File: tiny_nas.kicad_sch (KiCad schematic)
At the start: 110 parts, among them J1 Conn_02x07_Odd_Even, J2 DM3AT-SF-PEJM5, J3 USB_B_Micro, J4 Conn_01x02_Male, J5 HR911105A, J6 USB_B_Micro, J7 USB_B_Micro, J8 Conn_01x02_Male, J9 Conn_01x02_Male, SW1 SW_SPDT, U1 AMS1117-3.3, U2 LAN8720A, U3 STM32F407ZGTx, U4 USBLC6-4SC6, U5 USB3300-EZK, U6 MAX1823BEUB, U7 CH340E, Y1 16MHz, Y2 25MHz, Y3 24MHz

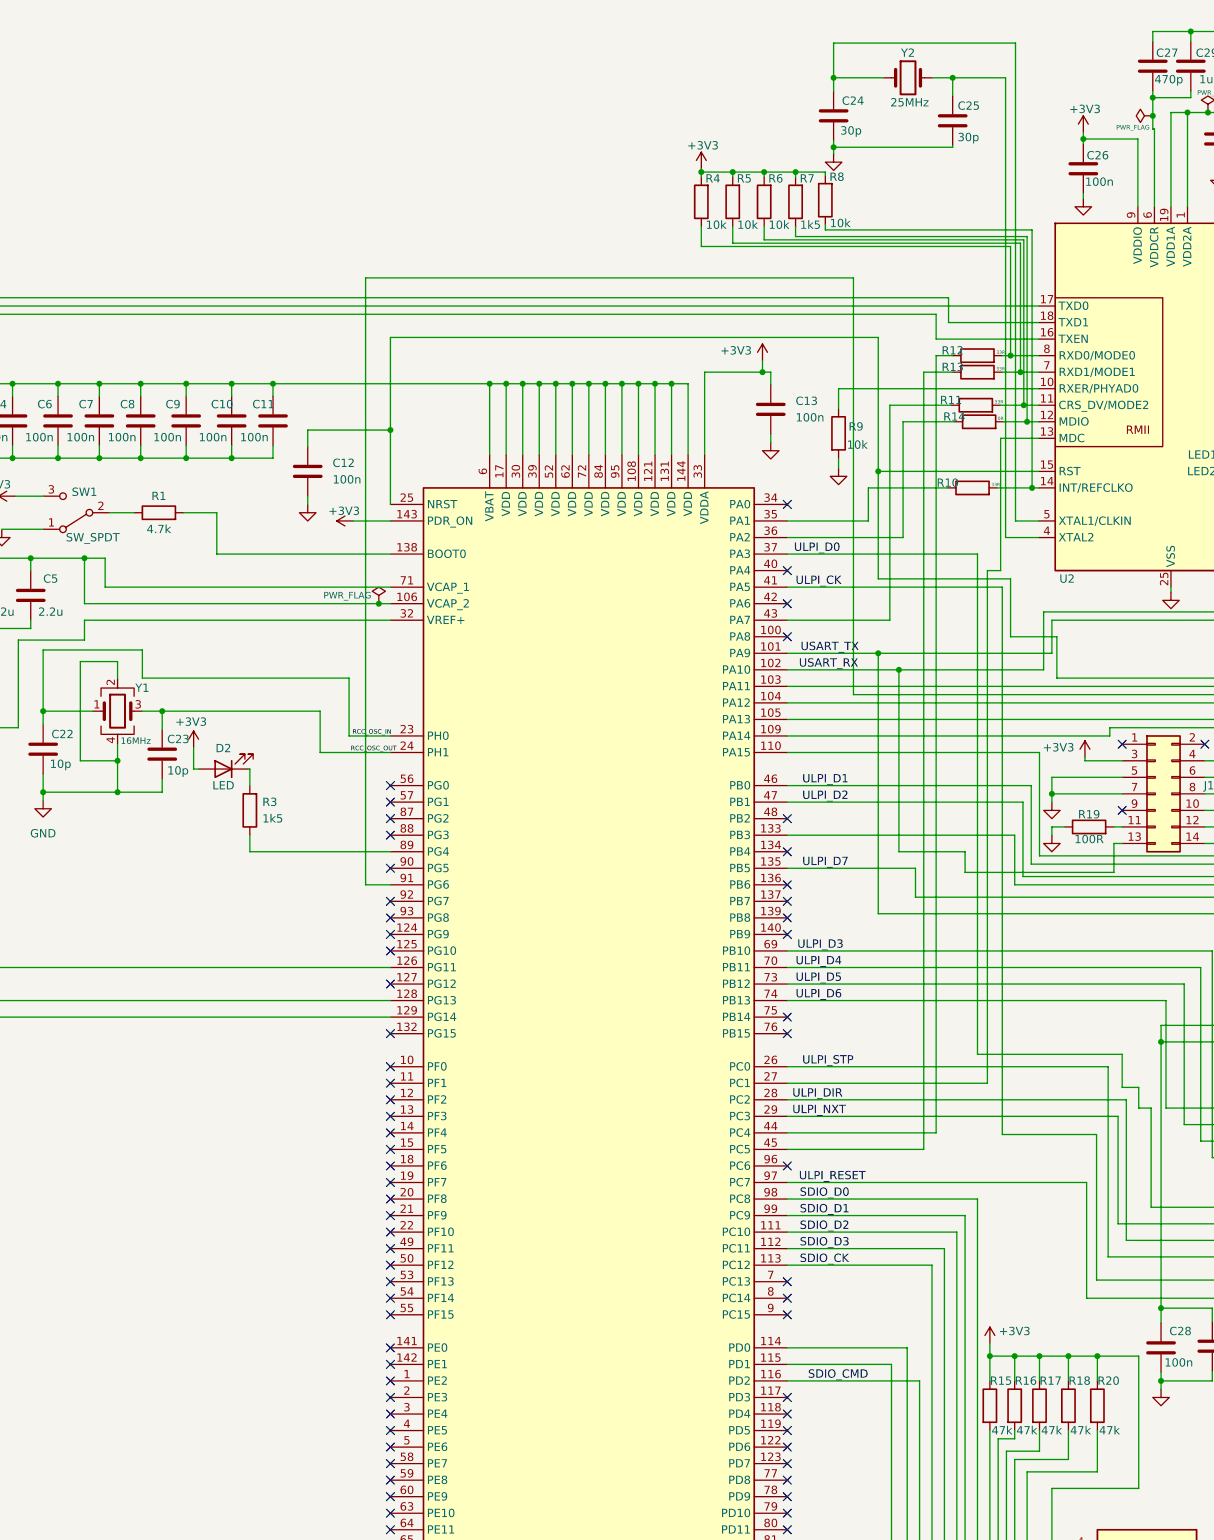
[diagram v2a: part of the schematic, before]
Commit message: Added Ethernet PHY reset GPIO and pin header to choose input clock from MCO or crystal
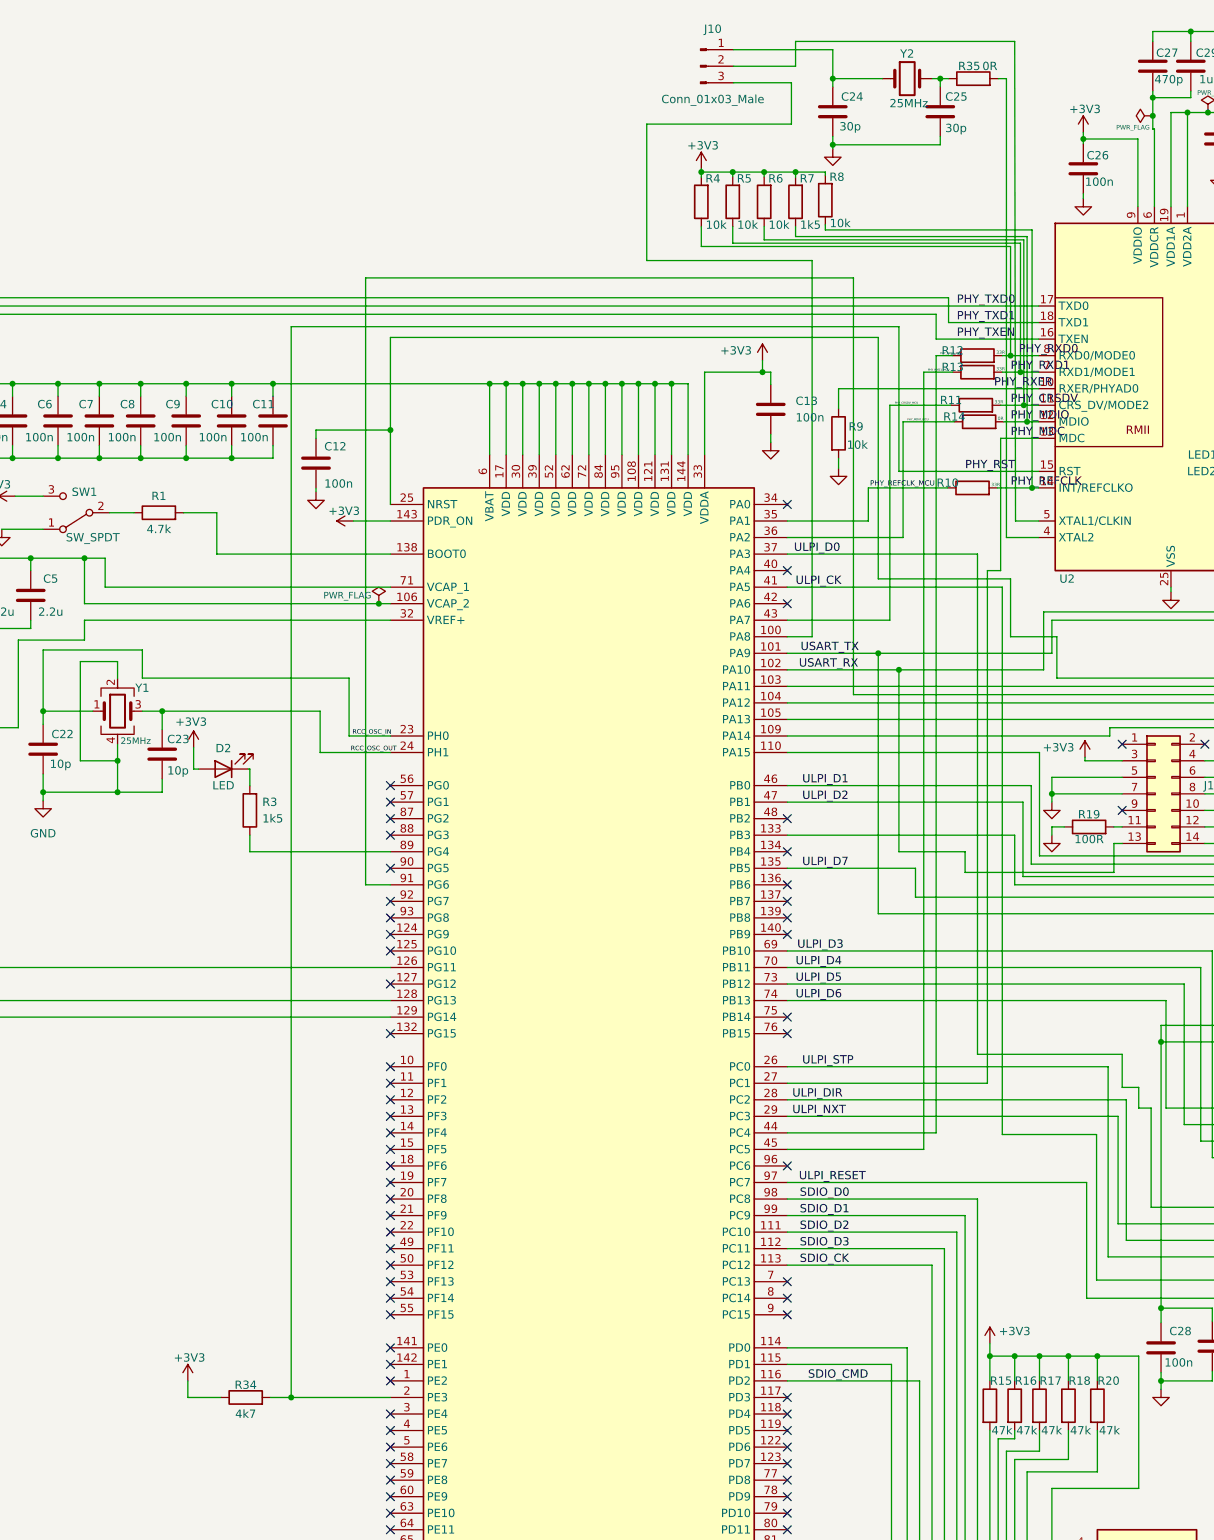
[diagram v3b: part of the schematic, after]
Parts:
- added J10: Conn_01x03_Male, Connector_PinHeader_2.54mm:PinHeader_1x03_P2.54mm_Vertical, symbol Connector:Conn_01x03_Male
- added R34: 4k7, Resistor_SMD:R_0402_1005Metric, symbol Device:R
- added R35: 0R, Resistor_SMD:R_0402_1005Metric, symbol Device:R
- Y1: value 16MHz -> 25MHz
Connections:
- net +3V3: now also R34.1
- net PHY_CRSDV_MCU: now reaches R11.1, U3.43 (PA7)
- net PHY_CRSDV: now reaches R11.2, R6.1, U2.11 (CRS_DV/MODE2)
- net PHY_RXD0_MCU: now reaches R12.1, U3.44 (PC4)
- net PHY_RXD0: now reaches R12.2, R4.1, U2.8 (RXD0/MODE0)
- net PHY_REFCLK_MCU: now reaches R10.1, U3.35 (PA1)
- net PHY_REFCLK: now reaches R10.2, R8.1, U2.14 (INT/REFCLKO)
- net at C12.2, J1.12 (Pin_12), U3.25 (NRST): no longer U2.15 (RST)
- net at C25.1, Y2.2: now also R35.1; no longer U2.4 (XTAL2)
- net PHY_RXER: now reaches R9.1, U2.10 (RXER/PHYAD0)
- net PHY_MDIO: now reaches R14.2, R7.1, U2.12 (MDIO)
- net PHY_MDC: now reaches U2.13 (MDC), U3.27 (PC1)
- net PHY_TXEN: now reaches U2.16 (TXEN), U3.126 (PG11)
- net PHY_TXD0: now reaches U2.17 (TXD0), U3.128 (PG13)
- net PHY_TXD1: now reaches U2.18 (TXD1), U3.129 (PG14)
- net at C24.1, Y2.1: now also J10.1 (Pin_1); no longer U2.5 (XTAL1/CLKIN)
- net PHY_RXD1: now reaches R13.2, R5.1, U2.7 (RXD1/MODE1)
- net PHY_MDIO_MCU: now reaches R14.1, U3.36 (PA2)
- net at U3.100 (PA8): now also J10.3 (Pin_3)
- net PHY_RST: now reaches U3.2 (PE3)
- net PHY_RST: now also U2.15 (RST), R34.2
- net PHY_RXD1_MCU: now reaches R13.1, U3.45 (PC5)
- new net: R35.2, U2.4 (XTAL2)
- new net: J10.2 (Pin_2), U2.5 (XTAL1/CLKIN)
- no-connect marks 84 -> 82
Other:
- moved on the sheet: C12, C24, C25

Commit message: change resistors footprint, add manufacturing files
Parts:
- R14, R26, R27, R30, R33, R35: footprint Resistor_SMD:R_0402_1005Metric -> Resistor_SMD:R_0603_1608Metric
- R22, R24, R25, R28: value 50R -> 49.9R; footprint Resistor_SMD:R_0402_1005Metric -> Resistor_SMD:R_0805_2012Metric
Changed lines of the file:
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@@
     (property "Reference" "R26" (id 0) (at 312.674 89.408 90))
     (property "Value" "270R" (id 1) (at 312.674 93.472 90))
-    (property "Footprint" "Resistor_SMD:R_0402_1005Metric" (id 2) (at 312.674 93.218 90)
+    (property "Footprint" "Resistor_SMD:R_0603_1608Metric" (id 2) (at 312.674 93.218 90)
       (effects (font (size 1.27 1.27)) hide)
     )
@@
       (effects (font (size 1.27 1.27)) (justify left))
     )
-    (property "Value" "50R" (id 1) (at 286.512 24.384 0)
-      (effects (font (size 1.27 1.27)) (justify left))
+    (property "Value" "49.9R" (id 1) (at 286.512 24.384 0)
+      (effects (font (size 1 1)) (justify left))
     )
-    (property "Footprint" "Resistor_SMD:R_0402_1005Metric" (id 2) (at 284.226 20.32 90)
+    (property "Footprint" "Resistor_SMD:R_0805_2012Metric" (id 2) (at 284.226 20.32 90)
       (effects (font (size 1.27 1.27)) hide)
     )
@@
       (effects (font (size 1.27 1.27)) (justify left))
     )
-    (property "Value" "50R" (id 1) (at 301.244 24.892 0)
-      (effects (font (size 1.27 1.27)) (justify left))
+    (property "Value" "49.9R" (id 1) (at 300.99 24.384 0)
+      (effects (font (size 0.8 0.8)) (justify left))
     )
-    (property "Footprint" "Resistor_SMD:R_0402_1005Metric" (id 2) (at 298.958 20.828 90)
+    (property "Footprint" "Resistor_SMD:R_0805_2012Metric" (id 2) (at 298.958 20.828 90)
       (effects (font (size 1.27 1.27)) hide)
     )
@@
     (property "Reference" "R33" (id 0) (at 327.406 198.628 90))
     (property "Value" "0R" (id 1) (at 327.406 202.692 90))
-    (property "Footprint" "Resistor_SMD:R_0402_1005Metric" (id 2) (at 327.406 202.438 90)
+    (property "Footprint" "Resistor_SMD:R_0603_1608Metric" (id 2) (at 327.406 202.438 90)
       (effects (font (size 1.27 1.27)) hide)
     )
@@
     (property "Reference" "R27" (id 0) (at 313.182 76.962 90))
     (property "Value" "270R" (id 1) (at 313.182 81.28 90))
-    (property "Footprint" "Resistor_SMD:R_0402_1005Metric" (id 2) (at 313.436 80.772 90)
+    (property "Footprint" "Resistor_SMD:R_0603_1608Metric" (id 2) (at 313.436 80.772 90)
       (effects (font (size 1.27 1.27)) hide)
     )
@@
       (effects (font (size 1.27 1.27)) (justify left))
     )
-    (property "Value" "50R" (id 1) (at 291.846 24.384 0)
-      (effects (font (size 1.27 1.27)) (justify left))
+    (property "Value" "49.9R" (id 1) (at 291.846 24.384 0)
+      (effects (font (size 1 1)) (justify left))
     )
-    (property "Footprint" "Resistor_SMD:R_0402_1005Metric" (id 2) (at 289.56 20.32 90)
+    (property "Footprint" "Resistor_SMD:R_0805_2012Metric" (id 2) (at 289.56 20.32 90)
       (effects (font (size 1.27 1.27)) hide)
     )
@@
       (effects (font (size 1.27 1.27)) (justify left))
     )
-    (property "Value" "50R" (id 1) (at 297.18 24.638 0)
-      (effects (font (size 1.27 1.27)) (justify left))
+    (property "Value" "49.9R" (id 1) (at 296.672 24.384 0)
+      (effects (font (size 0.8 0.8)) (justify left))
     )
-    (property "Footprint" "Resistor_SMD:R_0402_1005Metric" (id 2) (at 294.894 20.574 90)
+    (property "Footprint" "Resistor_SMD:R_0805_2012Metric" (id 2) (at 294.894 20.574 90)
       (effects (font (size 1.27 1.27)) hide)
     )
@@
       (effects (font (size 0.5 0.5)))
     )
-    (property "Footprint" "Resistor_SMD:R_0402_1005Metric" (id 2) (at 226.314 76.708 90)
+    (property "Footprint" "Resistor_SMD:R_0603_1608Metric" (id 2) (at 226.314 76.708 90)
       (effects (font (size 1.27 1.27)) hide)
     )
@@
     (property "Reference" "R30" (id 0) (at 325.755 168.275 90))
     (property "Value" "820R" (id 1) (at 332.105 168.275 90))
-    (property "Footprint" "Resistor_SMD:R_0402_1005Metric" (id 2) (at 328.93 171.958 90)
+    (property "Footprint" "Resistor_SMD:R_0603_1608Metric" (id 2) (at 328.93 171.958 90)
       (effects (font (size 1.27 1.27)) hide)
     )
@@
     (property "Reference" "R35" (id 0) (at 224.79 20.32 90))
     (property "Value" "0R" (id 1) (at 227.965 20.32 90))
-    (property "Footprint" "Resistor_SMD:R_0402_1005Metric" (id 2) (at 225.425 24.003 90)
+    (property "Footprint" "Resistor_SMD:R_0603_1608Metric" (id 2) (at 225.425 24.003 90)
       (effects (font (size 1.27 1.27)) hide)
     )
@@
     )
     (path "/c79aff15-50e4-4584-a522-8f6871a9a6a2"
-      (reference "R14") (unit 1) (value "0R") (footprint "Resistor_SMD:R_0402_1005Metric")
+      (reference "R14") (unit 1) (value "0R") (footprint "Resistor_SMD:R_0603_1608Metric")
     )
     (path "/9b7900c3-7805-4816-959c-97fecccbfcd1"
@@
     )
     (path "/10101c40-ff50-4600-a3ca-1c11c2497939"
-      (reference "R22") (unit 1) (value "50R") (footprint "Resistor_SMD:R_0402_1005Metric")
+      (reference "R22") (unit 1) (value "49.9R") (footprint "Resistor_SMD:R_0805_2012Metric")
     )
     (path "/e8ecb59c-9c02-4385-8b1f-27878130097a"
@@
     )
     (path "/adcec949-b9f9-436f-b1c2-bd46efd37af1"
-      (reference "R24") (unit 1) (value "50R") (footprint "Resistor_SMD:R_0402_1005Metric")
+      (reference "R24") (unit 1) (value "49.9R") (footprint "Resistor_SMD:R_0805_2012Metric")
     )
     (path "/c51582f8-7c92-4dce-9fcd-5430e77dacb0"
-      (reference "R25") (unit 1) (value "50R") (footprint "Resistor_SMD:R_0402_1005Metric")
+      (reference "R25") (unit 1) (value "49.9R") (footprint "Resistor_SMD:R_0805_2012Metric")
     )
     (path "/0eabe631-5b52-4ba2-a56a-8d4e4776cba9"
-      (reference "R26") (unit 1) (value "270R") (footprint "Resistor_SMD:R_0402_1005Metric")
+      (reference "R26") (unit 1) (value "270R") (footprint "Resistor_SMD:R_0603_1608Metric")
     )
     (path "/a3b91057-9fe5-4b82-ba33-0fba6cb83b77"
-      (reference "R27") (unit 1) (value "270R") (footprint "Resistor_SMD:R_0402_1005Metric")
+      (reference "R27") (unit 1) (value "270R") (footprint "Resistor_SMD:R_0603_1608Metric")
     )
     (path "/4396b126-6cd7-4e83-b2ef-794842d840c0"
-      (reference "R28") (unit 1) (value "50R") (footprint "Resistor_SMD:R_0402_1005Metric")
+      (reference "R28") (unit 1) (value "49.9R") (footprint "Resistor_SMD:R_0805_2012Metric")
     )
     (path "/9a36a1c7-b9b4-4cbd-8620-58095eb8b9a5"
@@
     )
     (path "/cfc53e2a-f0d1-490c-828f-574aab67facc"
-      (reference "R30") (unit 1) (value "820R") (footprint "Resistor_SMD:R_0402_1005Metric")
+      (reference "R30") (unit 1) (value "820R") (footprint "Resistor_SMD:R_0603_1608Metric")
     )
     (path "/9be72813-ab69-4999-b778-51f6a76732d9"
@@
     )
     (path "/6c34690a-3dfe-4cae-9f84-71399081064f"
-      (reference "R33") (unit 1) (value "0R") (footprint "Resistor_SMD:R_0402_1005Metric")
+      (reference "R33") (unit 1) (value "0R") (footprint "Resistor_SMD:R_0603_1608Metric")
     )
     (path "/7f1441d3-f66f-4b96-9d41-2f8025e38c7e"
@@
     )
     (path "/e77b989e-3290-450e-a681-afeecd7c7331"
-      (reference "R35") (unit 1) (value "0R") (footprint "Resistor_SMD:R_0402_1005Metric")
+      (reference "R35") (unit 1) (value "0R") (footprint "Resistor_SMD:R_0603_1608Metric")
     )
     (path "/ce442eff-9d39-4494-b02a-784b570d8422"
